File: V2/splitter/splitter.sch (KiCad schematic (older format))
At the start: 7 parts

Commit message: Identify control pins
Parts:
- added D0: LED_2V_20mA, symbol Device:LED
- added D1: 1N4007, symbol Device:D
- added K0: RELRAS0515, Relay_THT:Relay_SPDT_Finder_40.31, symbol Relay:FINDER-40.31
- added R0: 150R, symbol Device:R
- J0: renamed from J?; value Conn_02x20_Counter_Clockwise -> Rpi_40Pin_F; symbol Connector_Generic:Conn_02x20_Counter_Clockwise -> Connector_Generic:Conn_02x20_Odd_Even
- J1: renamed from J?; value Conn_02x03_Counter_Clockwise -> Control1_F
- J2: renamed from J?; value Conn_02x03_Counter_Clockwise -> Control2_F
- J3: renamed from J?; value Conn_02x03_Counter_Clockwise -> Control3_F
- J4: renamed from J?; value Conn_01x04 -> Molex_PSU_F
- J5: renamed from J?; value Screw_Terminal_01x02 -> Siren
- J6: renamed from J?; value USB_A -> USB_A_F
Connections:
- net labels added: 12V+, 1a, 1b, 1c, 1d, 2a, 2b, 2c, 2d, 3a, 3b, 3c, 3d, 5V+, BLANKING, Earth, GND
- wire segments 0 -> 36
- no-connect marks 0 -> 28
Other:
- moved on the sheet: J0, J1, J2, J3, J4, J5, J6

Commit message: Splitter schema
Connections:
- net labels added: SIREN
- wire segments 36 -> 73
- no-connect marks 28 -> 29
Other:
- moved on the sheet: D0, D1, J1, J2, J3, J4, J6, K0, R0

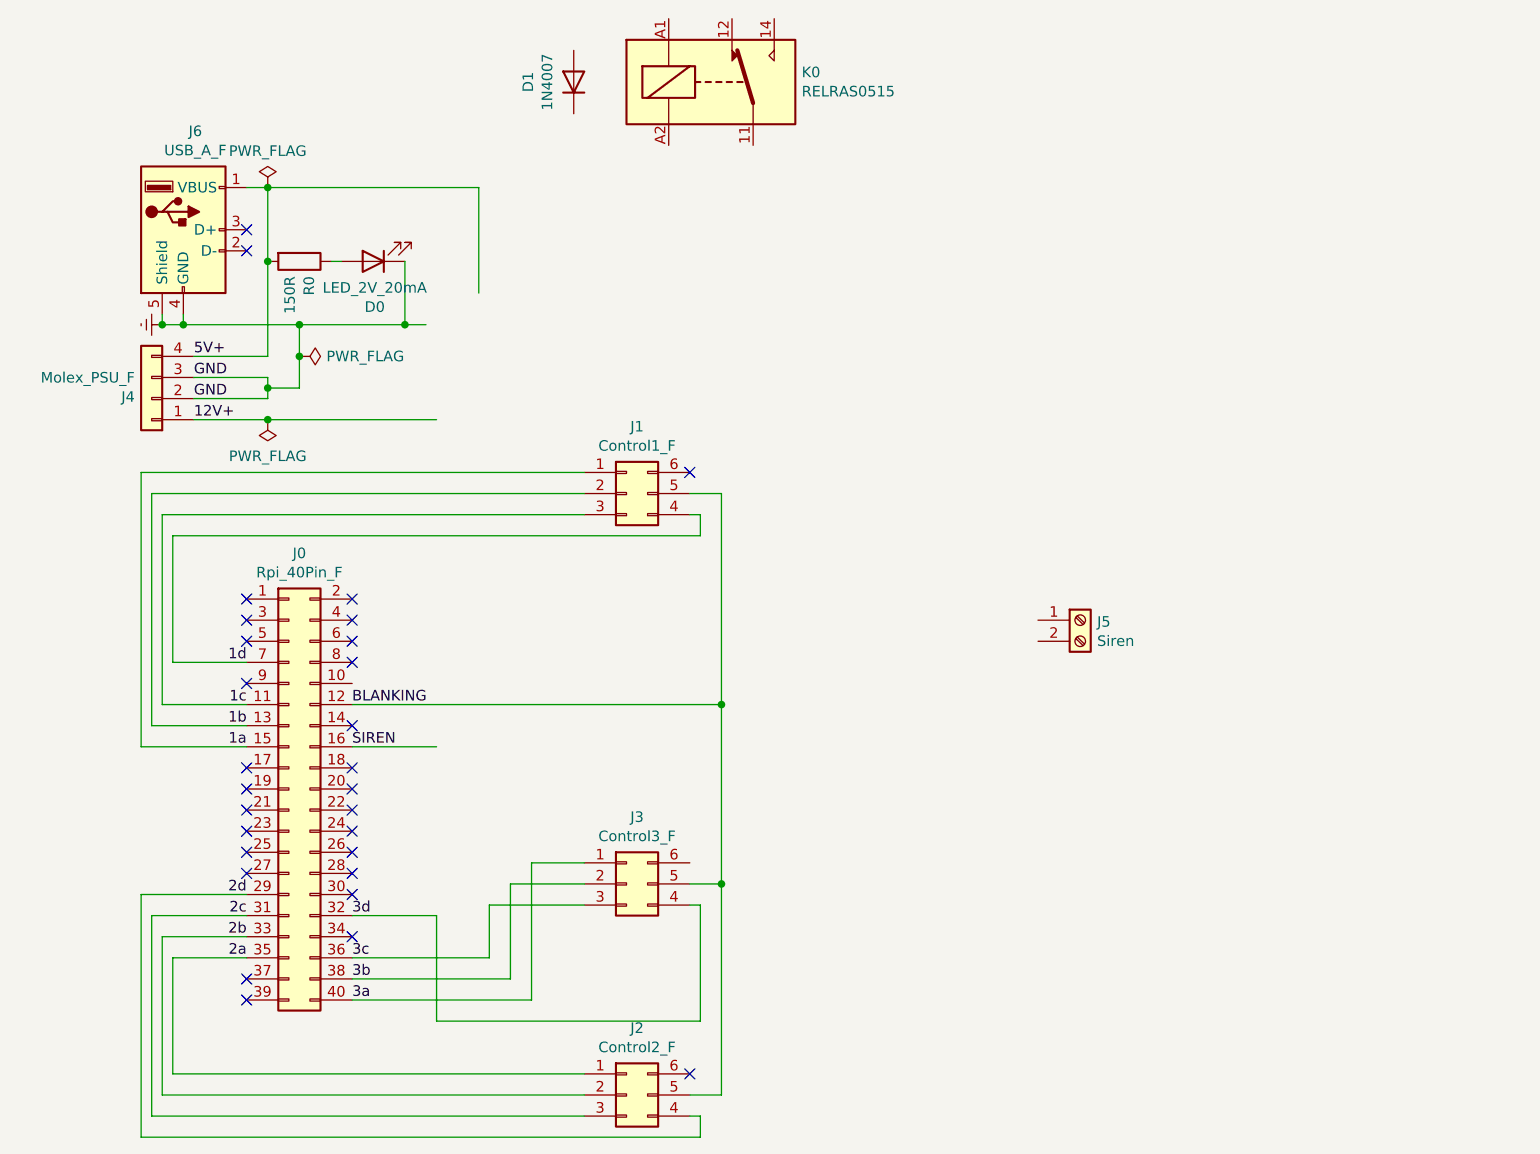
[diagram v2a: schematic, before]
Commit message: finish splitter schema
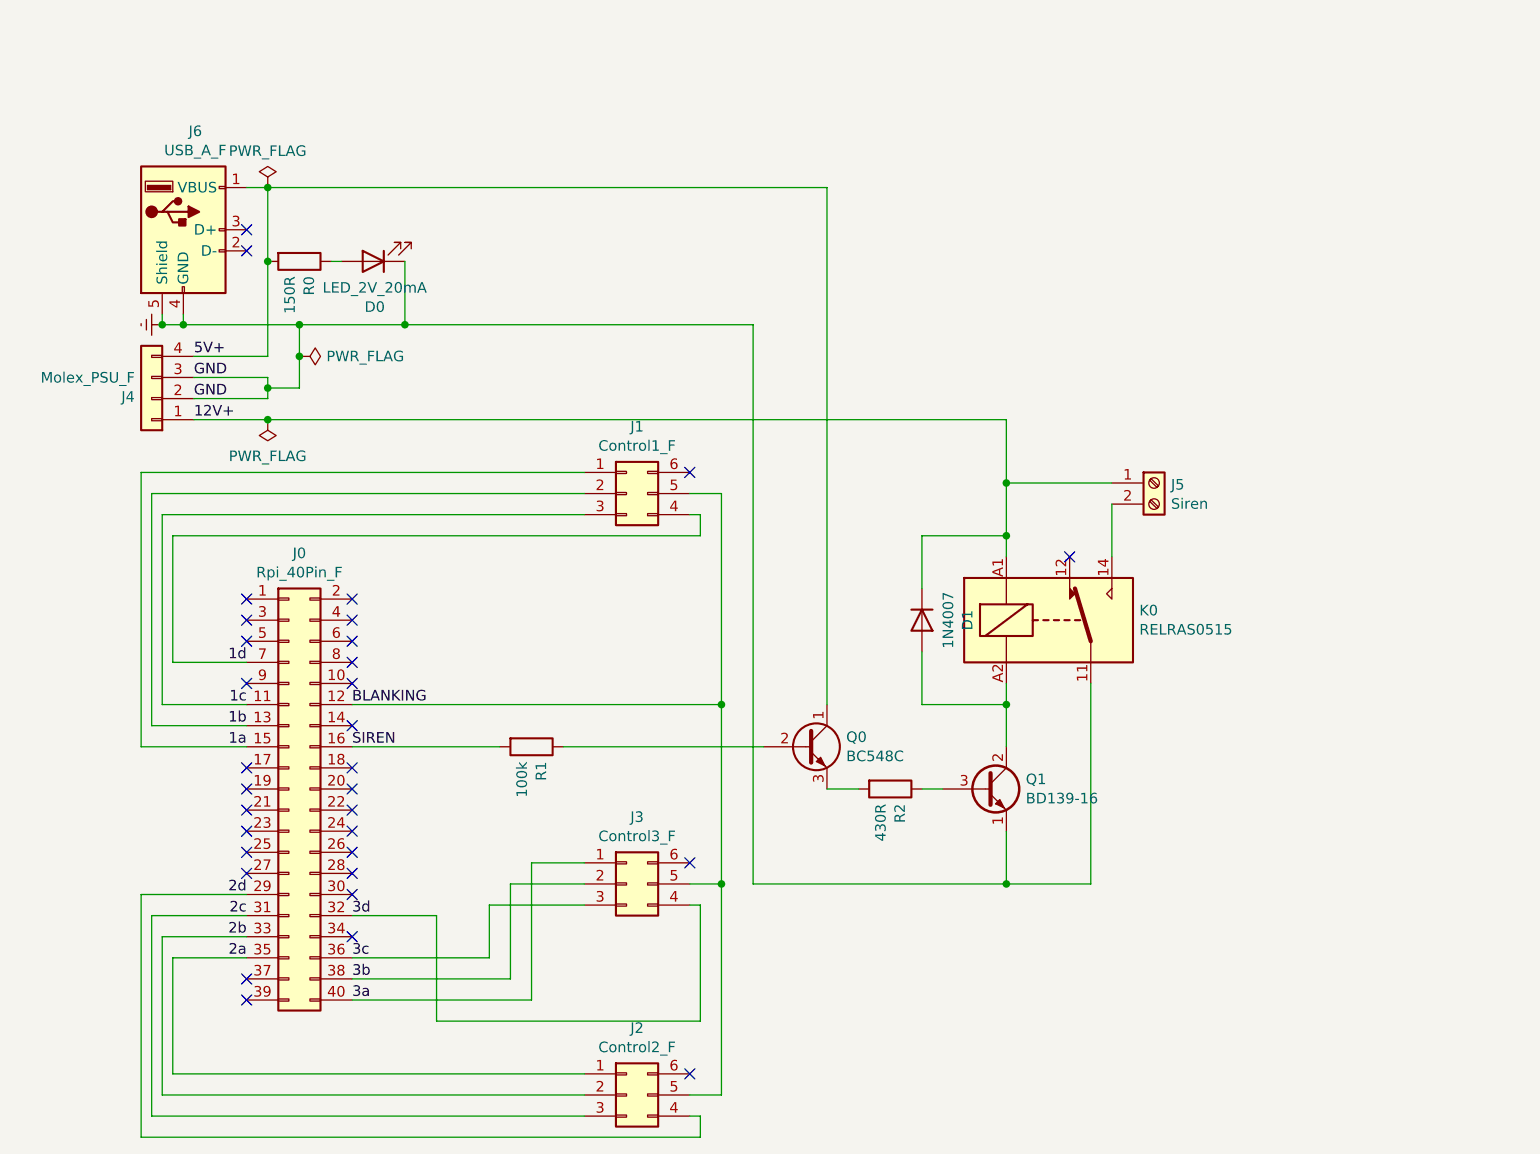
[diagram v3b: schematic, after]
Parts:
- added Q0: BC548C, Package_TO_SOT_THT:TO-92_Inline, symbol Transistor_BJT:BC548
- added Q1: BD139-16, Package_TO_SOT_THT:TO-126-3_Vertical, symbol Transistor_BJT:BD139
- added R1: 100k, symbol Device:R
- added R2: 430R, symbol Device:R
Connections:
- wire segments 73 -> 92
- no-connect marks 29 -> 32
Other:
- moved on the sheet: D1, J5, K0
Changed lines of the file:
@@
 L Connector:Screw_Terminal_01x02 J5
 U 1 1 5EBB14C8
-P 5600 3550
-F 0 "J5" H 5680 3542 50  0000 L CNN
-F 1 "Siren" H 5680 3451 50  0000 L CNN
-F 2 "" H 5600 3550 50  0001 C CNN
-F 3 "~" H 5600 3550 50  0001 C CNN
-	1    5600 3550
+P 5950 2900
+F 0 "J5" H 6030 2892 50  0000 L CNN
+F 1 "Siren" H 6030 2801 50  0000 L CNN
+F 2 "" H 5950 2900 50  0001 C CNN
+F 3 "~" H 5950 2900 50  0001 C CNN
+	1    5950 2900
 	1    0    0    -1
 $EndComp
@@
 L Device:D D1
 U 1 1 5EC1AB93
-P 3200 1000
-F 0 "D1" H 3200 1216 50  0000 C CNN
-F 1 "1N4007" H 3200 1125 50  0000 C CNN
-F 2 "" H 3200 1000 50  0001 C CNN
-F 3 "~" H 3200 1000 50  0001 C CNN
-	1    3200 1000
-	0    -1   -1   0
+P 4850 3550
+F 0 "D1" H 4850 3766 50  0000 C CNN
+F 1 "1N4007" H 4850 3675 50  0000 C CNN
+F 2 "" H 4850 3550 50  0001 C CNN
+F 3 "~" H 4850 3550 50  0001 C CNN
+	1    4850 3550
+	0    1    1    0
 $EndComp
 Text Label 1400 2600 0    50   ~ 0
@@
 	1900 2150 2400 2150
 Connection ~ 1900 2150
-Wire Wire Line
-	1750 2600 2550 2600
-Wire Wire Line
-	1750 1500 2750 1500
-Wire Wire Line
-	2750 1500 2750 2000
 Connection ~ 1750 1850
 Wire Wire Line
@@
 	2400 1850 2400 2150
 Connection ~ 2400 2150
-Wire Wire Line
-	2400 2150 2500 2150
 $Comp
 L power:PWR_FLAG #FLG0103
@@
 L Relay:FINDER-40.31 K0
 U 1 1 5ECA0675
-P 3850 1000
-F 0 "K0" H 4280 1046 50  0000 L CNN
-F 1 "RELRAS0515" H 4280 955 50  0000 L CNN
-F 2 "Relay_THT:Relay_SPDT_Finder_40.31" H 4990 960 50  0001 C CNN
-F 3 "http://gfinder.findernet.com/assets/Series/353/S40EN.pdf" H 3850 1000 50  0001 C CNN
-	1    3850 1000
+P 5450 3550
+F 0 "K0" H 5880 3596 50  0000 L CNN
+F 1 "RELRAS0515" H 5880 3505 50  0000 L CNN
+F 2 "Relay_THT:Relay_SPDT_Finder_40.31" H 6590 3510 50  0001 C CNN
+F 3 "http://gfinder.findernet.com/assets/Series/353/S40EN.pdf" H 5450 3550 50  0001 C CNN
+	1    5450 3550
 	1    0    0    -1
 $EndComp
@@
 SIREN
 Wire Wire Line
-	2150 4150 2550 4150
-Wire Wire Line
 	1300 3150 3800 3150
 Wire Wire Line
@@
 Wire Wire Line
 	2150 4950 2550 4950
+$Comp
+L Device:R R2
+U 1 1 5ED47928
+P 4700 4350
+F 0 "R2" H 4770 4396 50  0000 L CNN
+F 1 "430R" H 4770 4305 50  0000 L CNN
+F 2 "" V 4630 4350 50  0001 C CNN
+F 3 "~" H 4700 4350 50  0001 C CNN
+	1    4700 4350
+	0    1    1    0
+$EndComp
+$Comp
+L Transistor_BJT:BC548 Q0
+U 1 1 5ED48271
+P 4300 4150
+F 0 "Q0" H 4491 4196 50  0000 L CNN
+F 1 "BC548C" H 4491 4105 50  0000 L CNN
+F 2 "Package_TO_SOT_THT:TO-92_Inline" H 4500 4075 50  0001 L CIN
+F 3 "http://www.fairchildsemi.com/ds/BC/BC547.pdf" H 4300 4150 50  0001 L CNN
+	1    4300 4150
+	1    0    0    -1
+$EndComp
+$Comp
+L Transistor_BJT:BD139 Q1
+U 1 1 5ED492AC
+P 5150 4350
+F 0 "Q1" H 5342 4396 50  0000 L CNN
+F 1 "BD139-16" H 5342 4305 50  0000 L CNN
+F 2 "Package_TO_SOT_THT:TO-126-3_Vertical" H 5350 4275 50  0001 L CIN
+F 3 "http://www.st.com/internet/com/TECHNICAL_RESOURCES/TECHNICAL_LITERATURE/DATASHEET/CD00001225.pdf" H 5150 4350 50  0001 L CNN
+	1    5150 4350
+	1    0    0    -1
+$EndComp
+Wire Wire Line
+	2150 4150 2850 4150
+Wire Wire Line
+	3150 4150 4100 4150
+$Comp
+L Device:R R1
+U 1 1 5ED47212
+P 3000 4150
+F 0 "R1" H 3070 4196 50  0000 L CNN
+F 1 "100k" H 3070 4105 50  0000 L CNN
+F 2 "" V 2930 4150 50  0001 C CNN
+F 3 "~" H 3000 4150 50  0001 C CNN
+	1    3000 4150
+	0    1    1    0
+$EndComp
+Wire Wire Line
+	4400 1500 4400 3950
+Wire Wire Line
+	1750 1500 4400 1500
+Wire Wire Line
+	4550 4350 4400 4350
+Wire Wire Line
+	4850 4350 4950 4350
+Wire Wire Line
+	1750 2600 5250 2600
+Wire Wire Line
+	4050 2150 4050 4800
+Wire Wire Line
+	4050 4800 5250 4800
+Wire Wire Line
+	5250 4800 5250 4550
+Wire Wire Line
+	2400 2150 4050 2150
+Wire Wire Line
+	5250 3850 5250 3950
+Wire Wire Line
+	5250 2600 5250 2900
+Wire Wire Line
+	5250 3950 4850 3950
+Wire Wire Line
+	4850 3950 4850 3700
+Connection ~ 5250 3950
+Wire Wire Line
+	5250 3950 5250 4150
+Wire Wire Line
+	5250 3150 4850 3150
+Wire Wire Line
+	4850 3150 4850 3400
+Connection ~ 5250 3150
+Wire Wire Line
+	5250 3150 5250 3250
+Wire Wire Line
+	5750 2900 5250 2900
+Connection ~ 5250 2900
+Wire Wire Line
+	5250 2900 5250 3150
+Wire Wire Line
+	5750 3250 5750 3000
+Wire Wire Line
+	5650 3850 5650 4800
+Wire Wire Line
+	5650 4800 5250 4800
+Connection ~ 5250 4800
+NoConn ~ 5550 3250
+NoConn ~ 2150 3850
+NoConn ~ 3750 4700
 $EndSCHEMATC

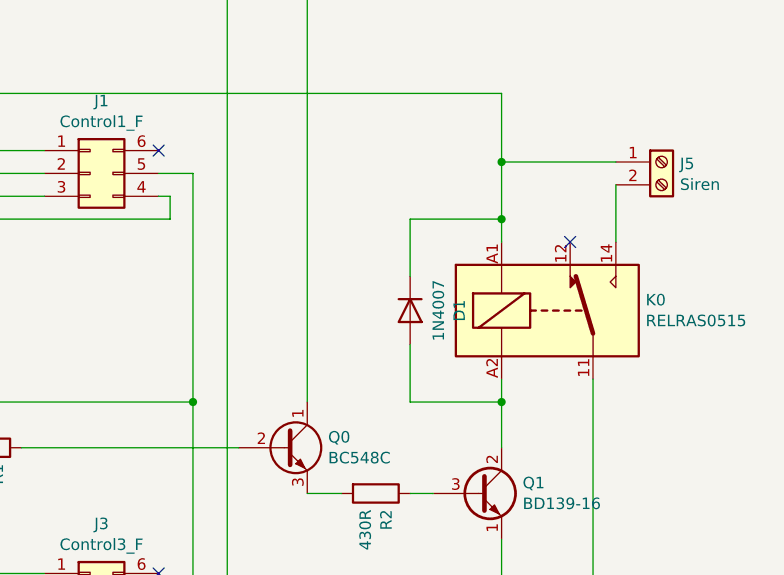
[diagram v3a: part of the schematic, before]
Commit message: Add control LED
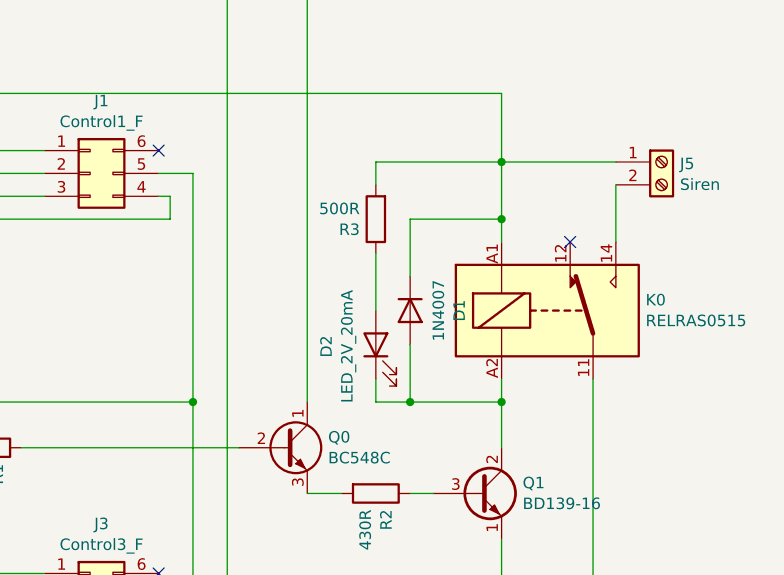
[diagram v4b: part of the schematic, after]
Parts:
- added D2: LED_2V_20mA, symbol Device:LED
- added R3: 500R, symbol Device:R
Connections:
- net 12V+: now also R3.2
- net at D1.2 (A), K0.A2, Q1.2 (C): now also D2.1 (K)
- new net: D2.2 (A), R3.1
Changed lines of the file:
@@
 NoConn ~ 2150 3850
 NoConn ~ 3750 4700
+$Comp
+L Device:LED D2
+U 1 1 5EDC36BC
+P 4700 3700
+F 0 "D2" H 4693 3916 50  0000 C CNN
+F 1 "LED_2V_20mA" H 4693 3825 50  0000 C CNN
+F 2 "" H 4700 3700 50  0001 C CNN
+F 3 "~" H 4700 3700 50  0001 C CNN
+	1    4700 3700
+	0    -1   -1   0
+$EndComp
+$Comp
+L Device:R R3
+U 1 1 5EDC8D2F
+P 4700 3150
+F 0 "R3" H 4770 3196 50  0000 L CNN
+F 1 "500R" H 4770 3105 50  0000 L CNN
+F 2 "" V 4630 3150 50  0001 C CNN
+F 3 "~" H 4700 3150 50  0001 C CNN
+	1    4700 3150
+	-1   0    0    1
+$EndComp
+Wire Wire Line
+	4700 3550 4700 3300
+Wire Wire Line
+	4700 3000 4700 2900
+Wire Wire Line
+	4700 2900 5250 2900
+Wire Wire Line
+	4700 3850 4700 3950
+Wire Wire Line
+	4700 3950 4850 3950
+Connection ~ 4850 3950
 $EndSCHEMATC

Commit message: Assign parts
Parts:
- D0, D2: footprint (none) -> LED_THT:LED_D5.0mm
- D1: footprint (none) -> Diode_THT:D_A-405_P10.16mm_Horizontal
- J0: footprint (none) -> Connector_PinHeader_2.54mm:PinHeader_2x20_P2.54mm_Vertical
- J1, J2, J3: footprint (none) -> Connector_PinHeader_2.54mm:PinHeader_2x03_P2.54mm_Horizontal
- J4: footprint (none) -> PSU:conn_hdd_15-24-4441
- J5: footprint (none) -> TerminalBlock:TerminalBlock_bornier-2_P5.08mm
- J6: footprint (none) -> Connector_USB:USB_A_Stewart_SS-52100-001_Horizontal
- R0, R1, R2, R3: footprint (none) -> Resistor_THT:R_Axial_DIN0207_L6.3mm_D2.5mm_P10.16mm_Horizontal
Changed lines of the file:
@@
 F 0 "J0" H 1900 5467 50  0000 C CNN
 F 1 "Rpi_40Pin_F" H 1900 5376 50  0000 C CNN
-F 2 "" H 1850 4350 50  0001 C CNN
+F 2 "Connector_PinHeader_2.54mm:PinHeader_2x20_P2.54mm_Vertical" H 1850 4350 50  0001 C CNN
 F 3 "~" H 1850 4350 50  0001 C CNN
 	1    1850 4350
@@
 F 0 "J1" H 3500 3267 50  0000 C CNN
 F 1 "Control1_F" H 3500 3176 50  0000 C CNN
-F 2 "" H 3450 2950 50  0001 C CNN
+F 2 "Connector_PinHeader_2.54mm:PinHeader_2x03_P2.54mm_Horizontal" H 3450 2950 50  0001 C CNN
 F 3 "~" H 3450 2950 50  0001 C CNN
 	1    3450 2950
@@
 F 0 "J2" H 3500 6117 50  0000 C CNN
 F 1 "Control2_F" H 3500 6026 50  0000 C CNN
-F 2 "" H 3450 5800 50  0001 C CNN
+F 2 "Connector_PinHeader_2.54mm:PinHeader_2x03_P2.54mm_Horizontal" H 3450 5800 50  0001 C CNN
 F 3 "~" H 3450 5800 50  0001 C CNN
 	1    3450 5800
@@
 F 0 "J3" H 3500 5117 50  0000 C CNN
 F 1 "Control3_F" H 3500 5026 50  0000 C CNN
-F 2 "" H 3450 4800 50  0001 C CNN
+F 2 "Connector_PinHeader_2.54mm:PinHeader_2x03_P2.54mm_Horizontal" H 3450 4800 50  0001 C CNN
 F 3 "~" H 3450 4800 50  0001 C CNN
 	1    3450 4800
@@
 F 0 "J4" H 1280 2492 50  0000 L CNN
 F 1 "Molex_PSU_F" H 1280 2401 50  0000 L CNN
-F 2 "" H 1200 2500 50  0001 C CNN
+F 2 "PSU:conn_hdd_15-24-4441" H 1200 2500 50  0001 C CNN
 F 3 "~" H 1200 2500 50  0001 C CNN
 	1    1200 2500
@@
 F 0 "J6" H 1407 2167 50  0000 C CNN
 F 1 "USB_A_F" H 1407 2076 50  0000 C CNN
-F 2 "" H 1500 1650 50  0001 C CNN
+F 2 "Connector_USB:USB_A_Stewart_SS-52100-001_Horizontal" H 1500 1650 50  0001 C CNN
 F 3 " ~" H 1500 1650 50  0001 C CNN
 	1    1350 1700
@@
 F 0 "J5" H 6030 2892 50  0000 L CNN
 F 1 "Siren" H 6030 2801 50  0000 L CNN
-F 2 "" H 5950 2900 50  0001 C CNN
+F 2 "TerminalBlock:TerminalBlock_bornier-2_P5.08mm" H 5950 2900 50  0001 C CNN
 F 3 "~" H 5950 2900 50  0001 C CNN
 	1    5950 2900
@@
 F 0 "R0" H 1970 1896 50  0000 L CNN
 F 1 "150R" H 1970 1805 50  0000 L CNN
-F 2 "" V 1830 1850 50  0001 C CNN
+F 2 "Resistor_THT:R_Axial_DIN0207_L6.3mm_D2.5mm_P10.16mm_Horizontal" V 1830 1850 50  0001 C CNN
 F 3 "~" H 1900 1850 50  0001 C CNN
 	1    1900 1850
@@
 F 0 "D0" H 2243 2066 50  0000 C CNN
 F 1 "LED_2V_20mA" H 2243 1975 50  0000 C CNN
-F 2 "" H 2250 1850 50  0001 C CNN
+F 2 "LED_THT:LED_D5.0mm" H 2250 1850 50  0001 C CNN
 F 3 "~" H 2250 1850 50  0001 C CNN
 	1    2250 1850
@@
 F 0 "D1" H 4850 3766 50  0000 C CNN
 F 1 "1N4007" H 4850 3675 50  0000 C CNN
-F 2 "" H 4850 3550 50  0001 C CNN
+F 2 "Diode_THT:D_A-405_P10.16mm_Horizontal" H 4850 3550 50  0001 C CNN
 F 3 "~" H 4850 3550 50  0001 C CNN
 	1    4850 3550
@@
 F 0 "R2" H 4770 4396 50  0000 L CNN
 F 1 "430R" H 4770 4305 50  0000 L CNN
-F 2 "" V 4630 4350 50  0001 C CNN
+F 2 "Resistor_THT:R_Axial_DIN0207_L6.3mm_D2.5mm_P10.16mm_Horizontal" V 4630 4350 50  0001 C CNN
 F 3 "~" H 4700 4350 50  0001 C CNN
 	1    4700 4350
@@
 F 0 "R1" H 3070 4196 50  0000 L CNN
 F 1 "100k" H 3070 4105 50  0000 L CNN
-F 2 "" V 2930 4150 50  0001 C CNN
+F 2 "Resistor_THT:R_Axial_DIN0207_L6.3mm_D2.5mm_P10.16mm_Horizontal" V 2930 4150 50  0001 C CNN
 F 3 "~" H 3000 4150 50  0001 C CNN
 	1    3000 4150
@@
 F 0 "D2" H 4693 3916 50  0000 C CNN
 F 1 "LED_2V_20mA" H 4693 3825 50  0000 C CNN
-F 2 "" H 4700 3700 50  0001 C CNN
+F 2 "LED_THT:LED_D5.0mm" H 4700 3700 50  0001 C CNN
 F 3 "~" H 4700 3700 50  0001 C CNN
 	1    4700 3700
@@
 F 0 "R3" H 4770 3196 50  0000 L CNN
 F 1 "500R" H 4770 3105 50  0000 L CNN
-F 2 "" V 4630 3150 50  0001 C CNN
+F 2 "Resistor_THT:R_Axial_DIN0207_L6.3mm_D2.5mm_P10.16mm_Horizontal" V 4630 3150 50  0001 C CNN
 F 3 "~" H 4700 3150 50  0001 C CNN
 	1    4700 3150

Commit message: swicth for avr
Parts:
- J6: symbol Connector:USB_A -> splitter-rescue:USB_A-Connector
- R3: value 500R -> 510R
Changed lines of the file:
@@
 $EndComp
 $Comp
-L Connector:USB_A J6
+L splitter-rescue:USB_A-Connector J6
 U 1 1 5EBB092E
 P 1350 1700
@@
 P 4700 3150
 F 0 "R3" H 4770 3196 50  0000 L CNN
-F 1 "500R" H 4770 3105 50  0000 L CNN
+F 1 "510R" H 4770 3105 50  0000 L CNN
 F 2 "Resistor_THT:R_Axial_DIN0207_L6.3mm_D2.5mm_P10.16mm_Horizontal" V 4630 3150 50  0001 C CNN
 F 3 "~" H 4700 3150 50  0001 C CNN
